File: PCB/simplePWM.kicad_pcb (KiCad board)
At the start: 2 copper layers, 50 x 40 mm, 34 parts, among them J1 POT, J2 VOUT, J3 ICSP, J4 Expansion, J5 TOGGLE, J6 PUSH, J7 VIN, Q1 PSMN7R5-30YLD, Q2 AO3401A, Q3 MMBT4401, U1 PIC16F18324-xSL, U2 L78L05_SOT89

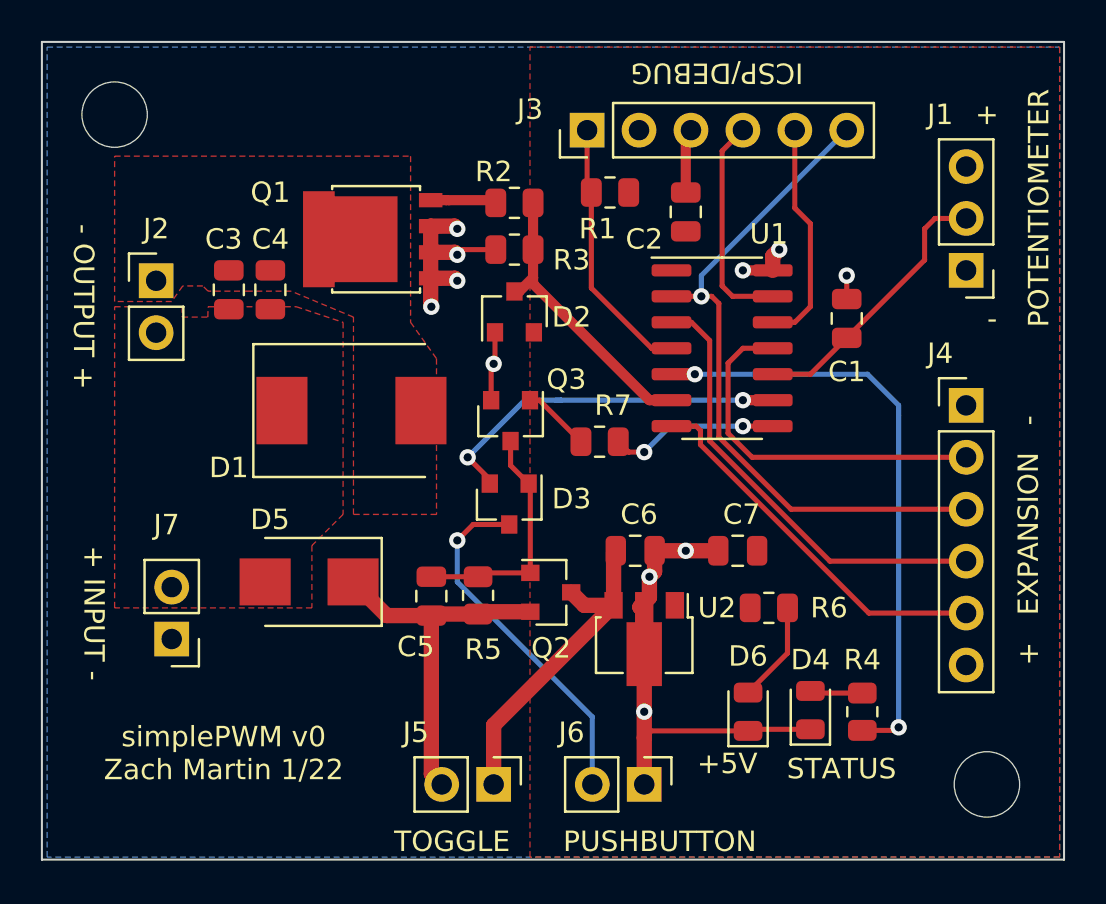
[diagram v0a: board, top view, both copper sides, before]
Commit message: Updated layout
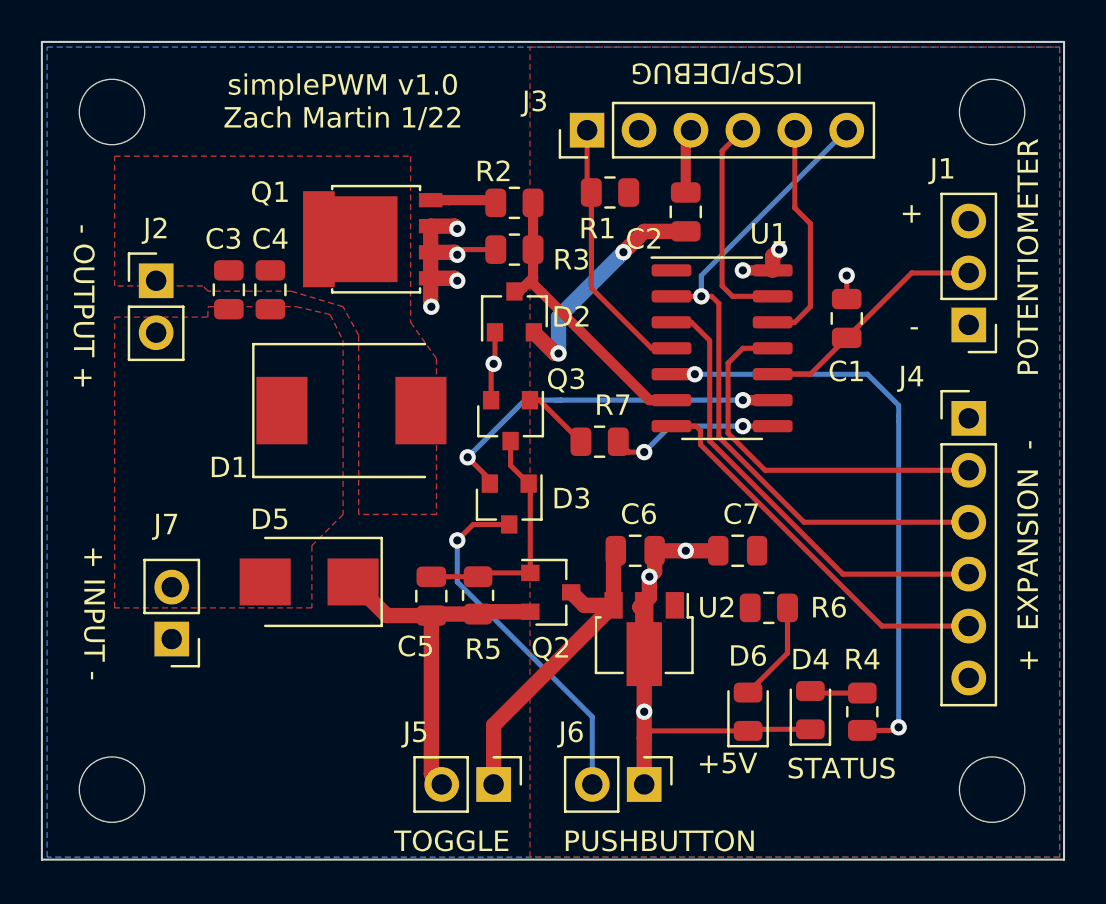
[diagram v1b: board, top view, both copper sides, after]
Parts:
- added H3: MountingHole, MountingHole:MountingHole_3.2mm_M3, F.Cu at (123.8, 113.5)
- added H4: MountingHole, MountingHole:MountingHole_3.2mm_M3, F.Cu at (166.9, 80.4)
- moved J1 2.67 mm to (165.7, 90.8)
- moved J4 0.65 mm to (165.7, 95.4)
- moved H2 0.36 mm to (166.9, 113.5)
- moved H1 0.18 mm to (123.8, 80.4)
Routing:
- net +5V: track 0.00 -> 11.4 mm, vias 0 -> 2
- net Net-(C1-Pad1): track 13.5 -> 11.6 mm
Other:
- board text added: "simplePWM v1.0 Zach Martin 1/22"
- board text removed: "simplePWM v0 Zach Martin 1/22"
